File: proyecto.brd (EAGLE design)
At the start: 95.8 x 48.2 mm, 42 parts, among them IC1 ADE9153AACPZ, J1 796638-3, K1 PR28-3V-360-1A-E, Q1 12.288M, Q2 BSS123, U1 ESP32-PICO-MINI-02-N8R2ESP32-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

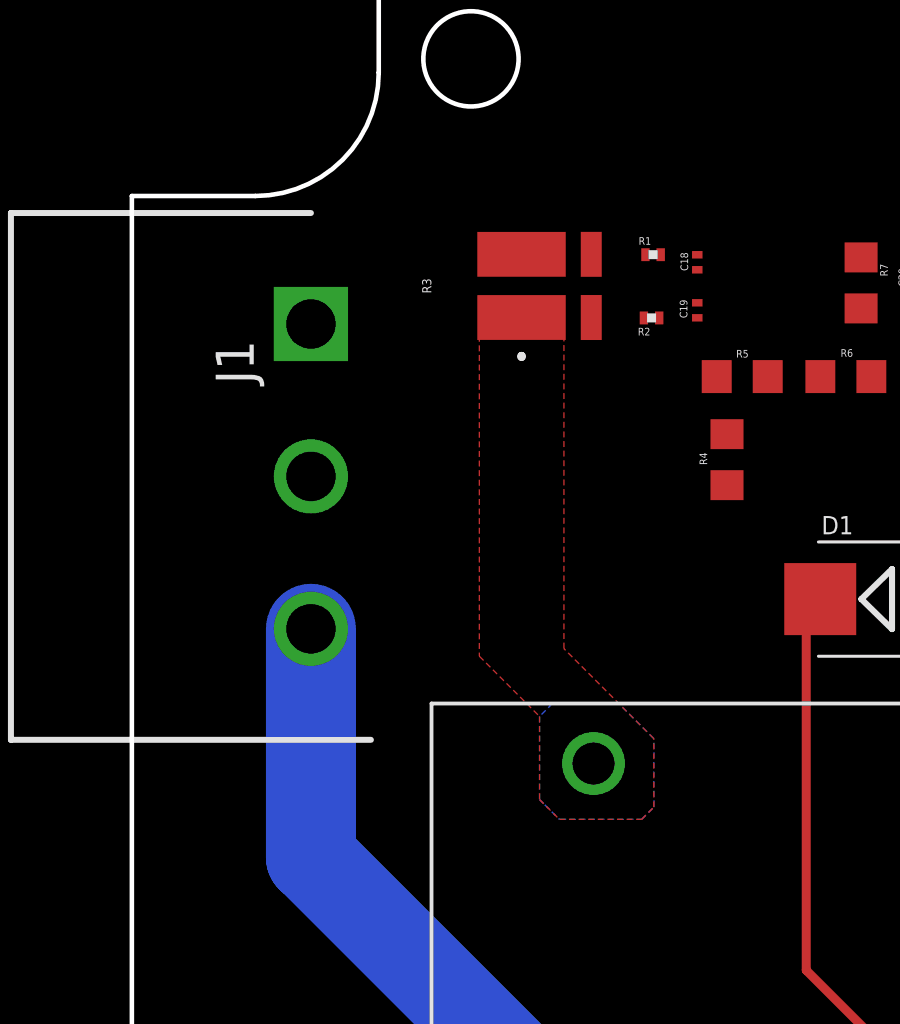
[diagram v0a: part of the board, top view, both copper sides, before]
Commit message: MINI avance
No se avanzó tanto debido a que se me daño las pistas en plena clase :(
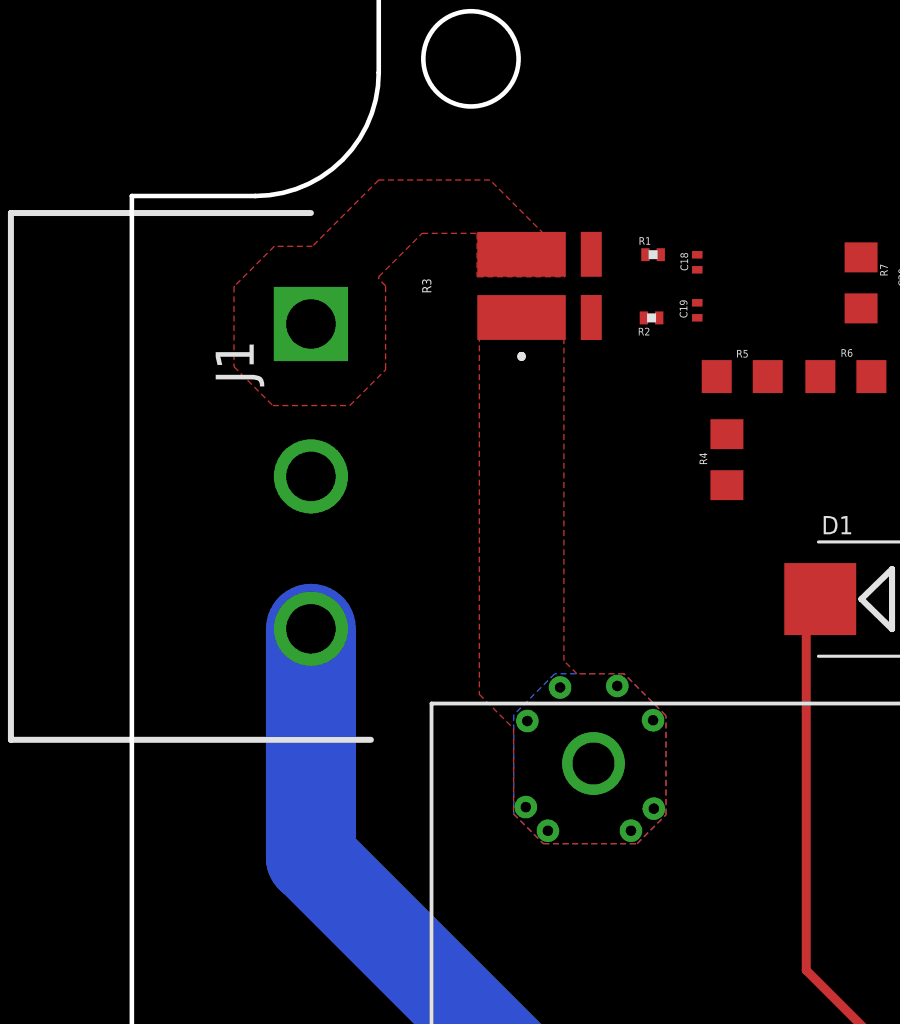
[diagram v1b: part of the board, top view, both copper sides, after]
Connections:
- net CARGA: now also R3.4
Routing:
- added copper zone on layer 1, net CARGA
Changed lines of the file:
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@@
 <drawing>
 <settings>
-<setting alwaysvectorfont="no"/>
+<setting alwaysvectorfont="yes"/>
 <setting verticaltext="up"/>
 </settings>
@@
 <signal name="CARGA">
 <contactref element="J1" pad="1"/>
+<contactref element="R3" pad="4"/>
+<polygon width="0.1524" layer="1" thermals="no">
+<vertex x="-36.3474" y="13.0048"/>
+<vertex x="-33.4518" y="13.0048"/>
+<vertex x="-33.4518" y="14.4272"/>
+<vertex x="-34.1376" y="14.4272"/>
+<vertex x="-35.941" y="16.2306"/>
+<vertex x="-39.6494" y="16.2306"/>
+<vertex x="-41.8592" y="14.0208"/>
+<vertex x="-43.1292" y="14.0208"/>
+<vertex x="-44.45" y="12.7"/>
+<vertex x="-44.4754" y="12.6746"/>
+<vertex x="-44.4754" y="10.0076"/>
+<vertex x="-43.18" y="8.7122"/>
+<vertex x="-40.6146" y="8.7122"/>
+<vertex x="-39.4208" y="9.906"/>
+<vertex x="-39.4208" y="9.9314"/>
+<vertex x="-39.4208" y="12.7"/>
+<vertex x="-39.6494" y="12.9286"/>
+<vertex x="-39.6494" y="13.0048"/>
+<vertex x="-38.2016" y="14.4526"/>
+<vertex x="-36.3728" y="14.4526"/>
+<vertex x="-36.3728" y="13.0048"/>
+</polygon>
 </signal>
 <signal name="NEUTRO">
@@
 <contactref element="R3" pad="1"/>
 <polygon width="0.15" layer="1" thermals="no" rank="2">
-<vertex x="-34.29" y="-1.651"/>
-<vertex x="-34.29" y="-4.4196"/>
-<vertex x="-33.629596875" y="-5.080003125"/>
-<vertex x="-30.886403125" y="-5.080003125"/>
-<vertex x="-30.48" y="-4.6736"/>
-<vertex x="-30.48" y="-2.3876"/>
-<vertex x="-33.4772" y="0.6096"/>
+<vertex x="-35.1536" y="-2.0574"/>
+<vertex x="-35.1536" y="-4.9022"/>
+<vertex x="-34.162996875" y="-5.892803125"/>
+<vertex x="-31.038803125" y="-5.892803125"/>
+<vertex x="-30.0736" y="-4.9276"/>
+<vertex x="-30.0736" y="-1.6256"/>
+<vertex x="-31.4706" y="-0.2286"/>
+<vertex x="-33.0454" y="-0.2286"/>
+<vertex x="-33.4772" y="0.2032"/>
 <vertex x="-33.4772" y="12.319"/>
 <vertex x="-36.2966" y="12.319"/>
-<vertex x="-36.2966" y="0.3556"/>
+<vertex x="-36.2966" y="-0.9144"/>
 </polygon>
 <polygon width="0.15" layer="16" thermals="no">
-<vertex x="-34.29" y="-1.651"/>
-<vertex x="-34.29" y="-4.4196"/>
-<vertex x="-34.1122" y="-4.5974"/>
-<vertex x="-33.6296" y="-5.08"/>
-<vertex x="-33.6042" y="-5.08"/>
-<vertex x="-30.8864" y="-5.08"/>
-<vertex x="-30.48" y="-4.6736"/>
-<vertex x="-30.48" y="-4.6482"/>
-<vertex x="-30.48" y="-2.3876"/>
-<vertex x="-31.6484" y="-1.2192"/>
-<vertex x="-33.5026" y="-1.2192"/>
-<vertex x="-33.8582" y="-1.2192"/>
+<vertex x="-35.1536" y="-1.6002"/>
+<vertex x="-35.1536" y="-4.9022"/>
+<vertex x="-34.163" y="-5.8928"/>
+<vertex x="-31.0388" y="-5.8928"/>
+<vertex x="-30.0736" y="-4.9276"/>
+<vertex x="-30.0736" y="-1.6256"/>
+<vertex x="-31.4706" y="-0.2286"/>
+<vertex x="-33.782" y="-0.2286"/>
 </polygon>
 </signal>
+<signal name="N$15">
+<via x="-34.6964" y="-1.8034" extent="1-16" drill="0.35"/>
+</signal>
+<signal name="N$16">
+<via x="-33.6042" y="-0.6858" extent="1-16" drill="0.35"/>
+</signal>
+<signal name="N$17">
+<via x="-31.6992" y="-0.635" extent="1-16" drill="0.35"/>
+</signal>
+<signal name="N$18">
+<via x="-30.5054" y="-1.778" extent="1-16" drill="0.35"/>
+</signal>
+<signal name="N$19">
+<via x="-30.48" y="-4.7244" extent="1-16" drill="0.35"/>
+</signal>
+<signal name="N$20">
+<via x="-31.242" y="-5.461" extent="1-16" drill="0.35"/>
+</signal>
+<signal name="N$21">
+<via x="-34.0106" y="-5.461" extent="1-16" drill="0.35"/>
+</signal>
+<signal name="N$22">
+<via x="-34.7472" y="-4.6736" extent="1-16" drill="0.35"/>
+</signal>
 </signals>

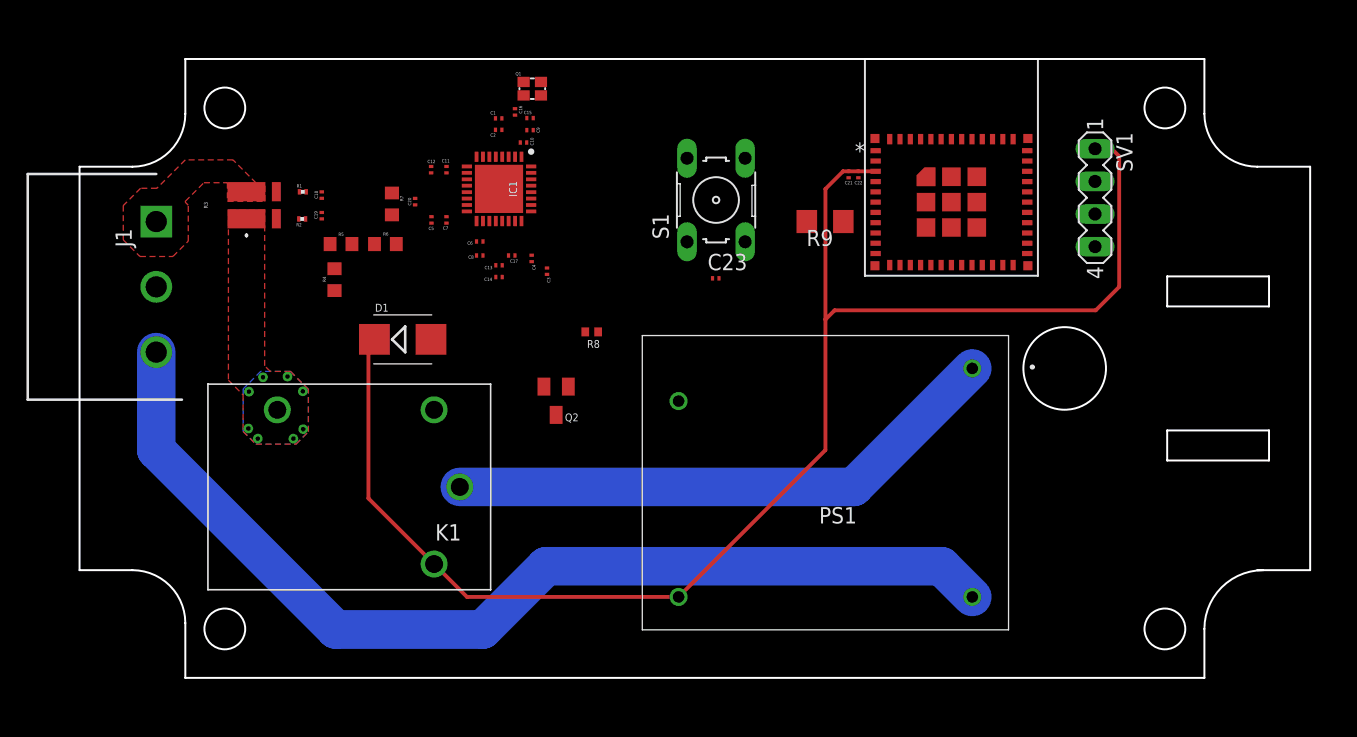
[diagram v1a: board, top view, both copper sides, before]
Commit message: Se añado y arreglo pistas
Se arreglo las pistas de la fase y el neutro en las clavijas. Se añadieron otras pistas y se quito el boton del enable.
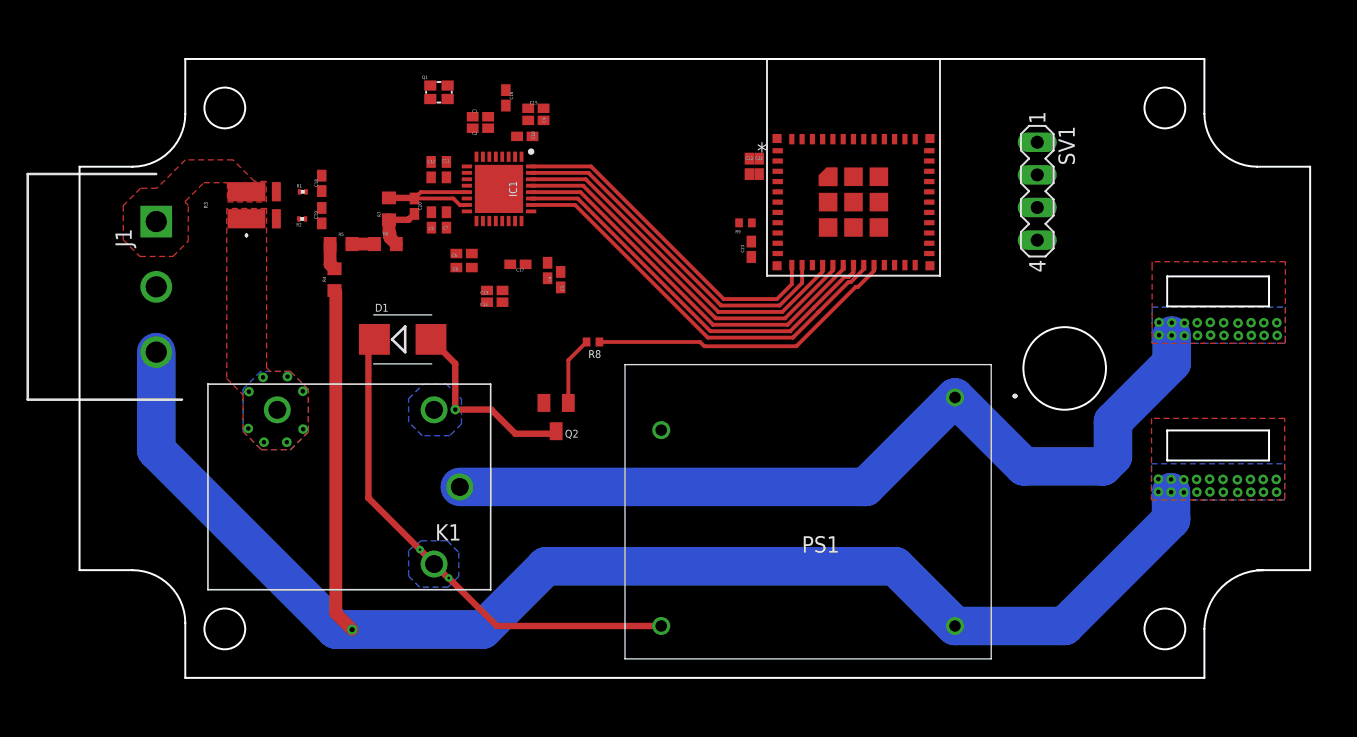
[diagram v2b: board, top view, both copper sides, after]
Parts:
- removed S1: (no value), switch-omron:B3F-10XX
- C1, C10, C11, C12, C13, C14, C15, C16, C17, C18, C19, C2, C20, C21, C22, C23, C3, C4, C5, C6, C7, C8, C9: device rcl:C0201 -> rcl:C0402K
- R9: device rcl:R1206 -> rcl:R0402
- moved C22 8.51 mm to (4.24, 15.7), turned to 90 degrees
- moved U1 7.62 mm to (12.3, 15.6)
- moved Q1 7.27 mm to (-19.9, 21.5)
- moved C21 6.99 mm to (5.00, 15.7), turned to 90 degrees
- moved R9 6.20 mm to (3.94, 11.3), turned to 0 degrees
- moved SV1 4.52 mm to (26.6, 13.8)
- moved C23 3.57 mm to (4.39, 9.27), turned to 270 degrees
- moved PS1 2.63 mm to (20.2, -2.26)
- moved C13 1.98 mm to (-15.6, 6.07)
- moved C14 1.98 mm to (-15.6, 5.16)
- moved C4 1.56 mm to (-11.5, 7.62)
- moved C6 1.54 mm to (-18.0, 8.94)
- moved C8 1.54 mm to (-18.0, 7.85)
- moved C1 1.43 mm to (-16.7, 19.6)
- moved C2 1.43 mm to (-16.7, 18.7)
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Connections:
- removed net N$14: C23.1, R9.2, S1.1
- net +3V3: now also R9.1
- net CF1: now also U1.19
- net EN: now also C23.1, R9.2; no longer R9.1
- net GND: now also U1.1, U1.11, U1.14, U1.2, U1.36, U1.37, U1.38, U1.39, U1.40, U1.41, U1.42, U1.43, U1.44, U1.45, U1.46, U1.47, U1.48, U1.49, U1.50, U1.51, U1.52, U1.53, U1.54, U1.55, U1.56, U1.57, U1.58, U1.59, U1.60, U1.61; no longer S1.3
- net IRQ: now also U1.18
- net NEUTRO: now also R4.1
- net RELAY_CONTROL: now also U1.20
- net RESET: now also U1.17
- net RX: now also U1.16
- net SCLK: now also U1.13; no longer U1.5
- net SS: now also U1.12; no longer U1.4
- net TX: now also U1.15
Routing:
- net +3V3: track 115.8 -> 38.3 mm, vias 0 -> 2
- net NEUTRO: track 79.9 -> 128.8 mm, vias 0 -> 21
- net CF1: track 0.00 -> 32.7 mm
- net IRQ: track 0.00 -> 31.8 mm
- net RESET: track 0.00 -> 30.7 mm
- net RX: track 0.00 -> 29.7 mm
- net TX: track 0.00 -> 28.8 mm
- net SCLK: track 0.00 -> 27.5 mm
- net SS: track 0.00 -> 26.5 mm
- net RELAY_CONTROL: track 0.00 -> 24.4 mm
- net LINEA: track 43.7 -> 67.5 mm, vias 0 -> 20
- net RELAY: track 0.00 -> 15.0 mm, vias 0 -> 1
- net N$10: track 0.00 -> 10.6 mm
- net N$13: track 0.00 -> 5.33 mm
- net N$9: track 0.00 -> 4.30 mm
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- added copper zone on layer 16, net +3V3
- added copper zone on layer 1, net LINEA
- added copper zone on layer 16, net LINEA
- added copper zone on layer 1, net NEUTRO
- added copper zone on layer 16, net NEUTRO
- added copper zone on layer 16, net RELAY

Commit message: Terminada la mayoria de conexiones
Se realizo la gran mayoria de las conexiones, falta realizar las conexiones especificadas en el DRC.
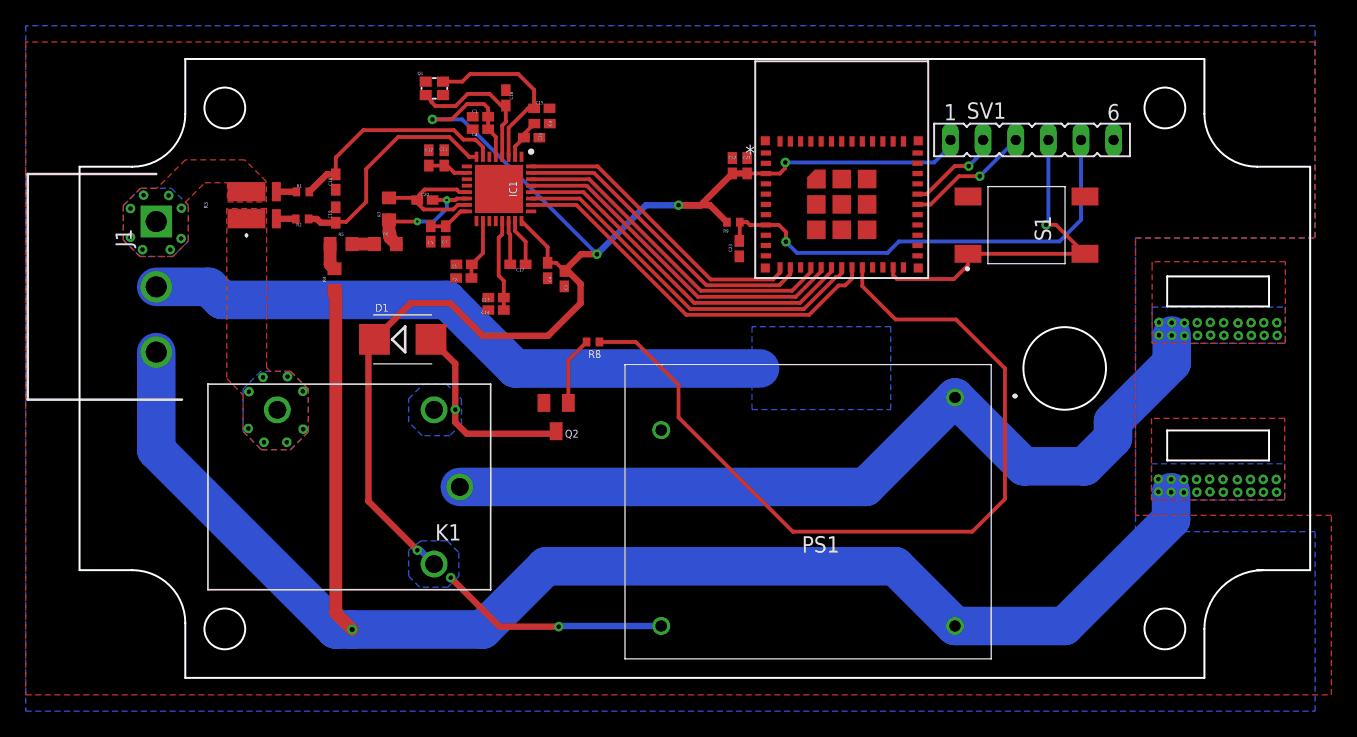
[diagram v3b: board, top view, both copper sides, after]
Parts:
- added S1: 3-1437565-0, SamacSys_Parts:314375650
- R1, R2: device rcl:R0201 -> rcl:R0402
- SV1: device con-lstb:MA04-1 -> con-lsta:FE06
- moved SV1 4.01 mm to (26.2, 17.8), turned to 0 degrees
- moved C22 1.32 mm to (2.92, 15.8)
- moved C18 1.10 mm to (-27.9, 14.5)
- moved C5 1.09 mm to (-20.5, 10.5)
- moved C7 1.09 mm to (-19.4, 10.5)
- moved C19 1.09 mm to (-27.9, 11.9)
- moved C20 0.95 mm to (-21.0, 13.1), turned to 0 degrees
- moved C21 0.94 mm to (4.06, 15.8)
- moved R9 0.94 mm to (3.00, 11.4)
- moved C23 0.94 mm to (3.45, 9.32)
- moved U1 0.93 mm to (11.4, 15.5)
- moved C11 0.93 mm to (-19.5, 16.4)
- moved C12 0.93 mm to (-20.7, 16.4)
- moved C6 0.84 mm to (-18.0, 8.10)
- moved C8 0.81 mm to (-18.0, 7.04)
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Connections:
- net CARGA_M renamed MONDA
- net N$11 renamed PROG_TX
- net N$12 renamed PROG_RX
- removed net VDD1: C1.1, C2.1, IC1.5
- removed net VDD2: C3.1, C4.1, IC1.24
- new net BOOT: S1.1, S1.2, SV1.4, U1.23
- net +3V3: now also C1.1, C2.1, C3.1, C4.1, IC1.24, IC1.5
- net EN: now also SV1.5
- net GND: now also S1.3, S1.4, SV1.6; no longer SV1.4
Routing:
- net +3V3: track 38.3 -> 131.3 mm, vias 2 -> 7
- net TIERRA: track 0.00 -> 49.6 mm
- net RELAY_CONTROL: track 24.4 -> 65.6 mm
- net EN: track 0.00 -> 36.7 mm, vias 0 -> 1
- net BOOT: track 0.00 -> 27.7 mm, vias 0 -> 1
- net N$5: track 0.00 -> 18.1 mm
- net N$3: track 0.00 -> 17.6 mm
- net CLKOUT: track 0.00 -> 14.1 mm
- net CLKIN: track 0.00 -> 11.5 mm
- net PROG_RX: track 0.00 -> 9.73 mm, vias 0 -> 1
- net PROG_TX: track 0.00 -> 7.38 mm, vias 0 -> 1
- net MSH: track 0.00 -> 7.20 mm
- net N$9: track 4.30 -> 10.5 mm, vias 0 -> 2
- net REFIN: track 0.00 -> 4.80 mm
- net N$1: track 0.00 -> 3.71 mm
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- added copper zone on layer 16, net CARGA
- added copper zone on layer 1, net GND
- added copper zone on layer 16, net GND
- added copper zone on layer 16, net TIERRA

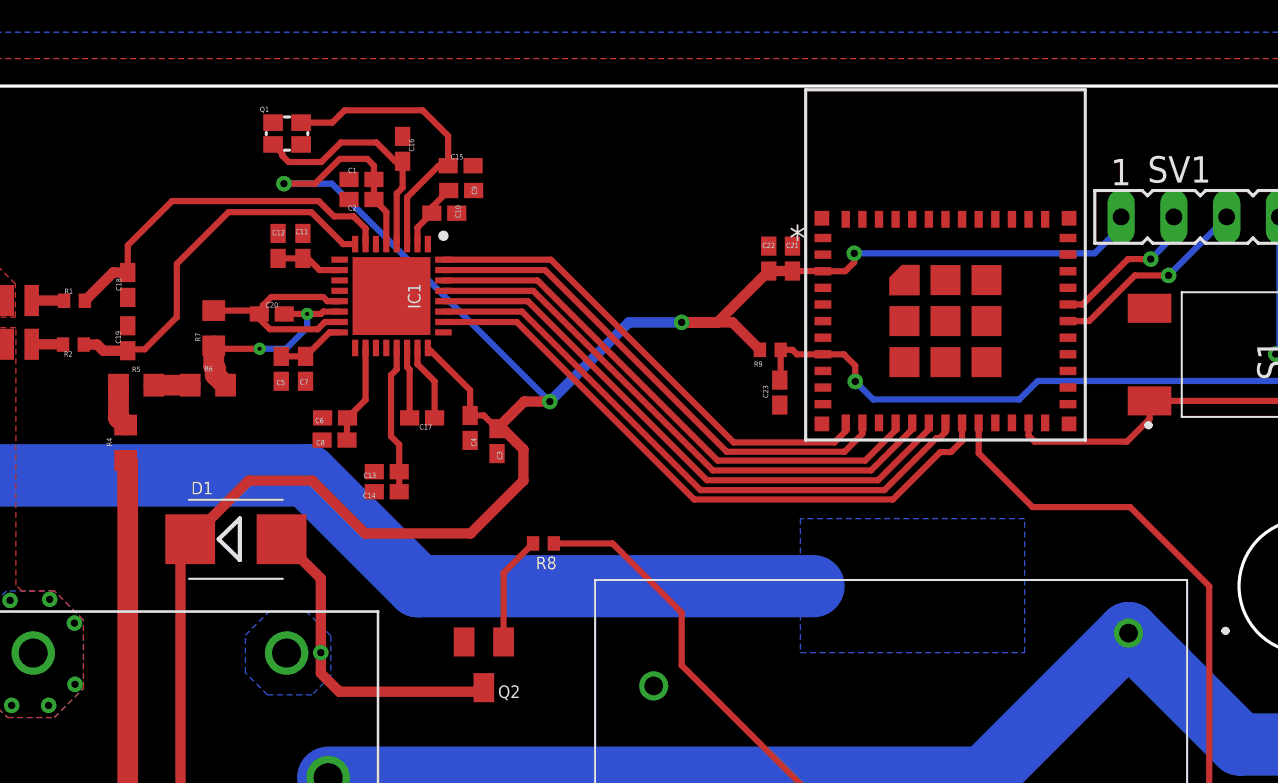
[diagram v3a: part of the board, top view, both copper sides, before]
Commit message: Errores DRC solucionados
Se revisaron los errores DRC acerca de las conexiones faltantes. Ya no hay errores DRC. Falta montar diodos led indicativos y cambiar el boton de boot de ser necesario
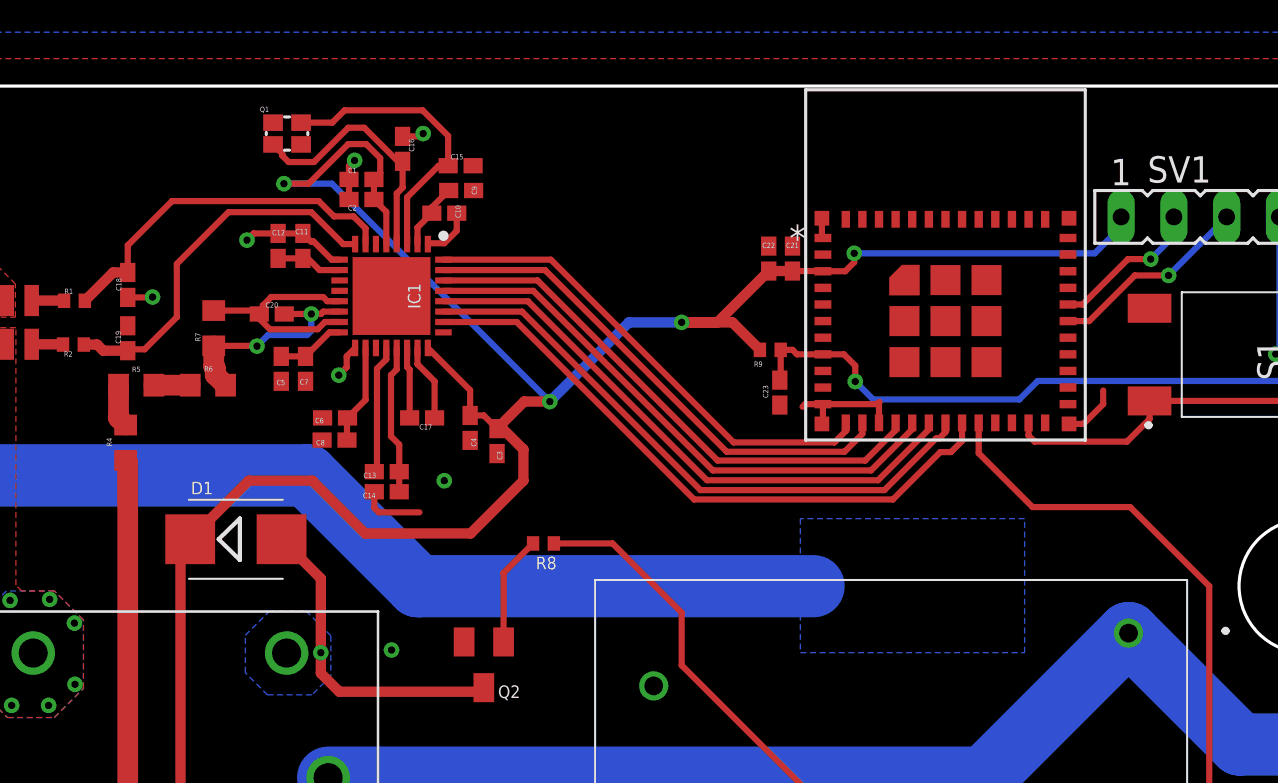
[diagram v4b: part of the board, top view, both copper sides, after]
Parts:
- R1, R2: value 150k -> 150
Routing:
- net GND: track 0.00 -> 32.1 mm, vias 0 -> 7
- net +3V3: track 131.3 -> 132.6 mm
- net CLKIN: track 11.5 -> 12.1 mm
